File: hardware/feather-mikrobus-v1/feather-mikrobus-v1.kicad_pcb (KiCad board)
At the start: 2 copper layers, 63.5 x 58.4 mm, 26 parts, among them J1 Adafruit_Feather_socket_heade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, J2 Adafruit_Feather_socket_heade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, J3 mikroBUS_socket_header_left_p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, J4 mikroBUS_socket_header_right_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, SW1 C_and_K_JS102011SAQN, SW2 C_and_K_KMR421GULCLFS, SW3 C_and_K_KMR421GULCLFS

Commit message: Add Flying Camp Design logo
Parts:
- added LOGO2: Flying_Camp_Design_logo_30x30mm_silkscreen, Flying_Camp_Design:Flying_Camp_Design_logo_30x30mm_silkscreen, B.Cu at (156.2, 128.3)

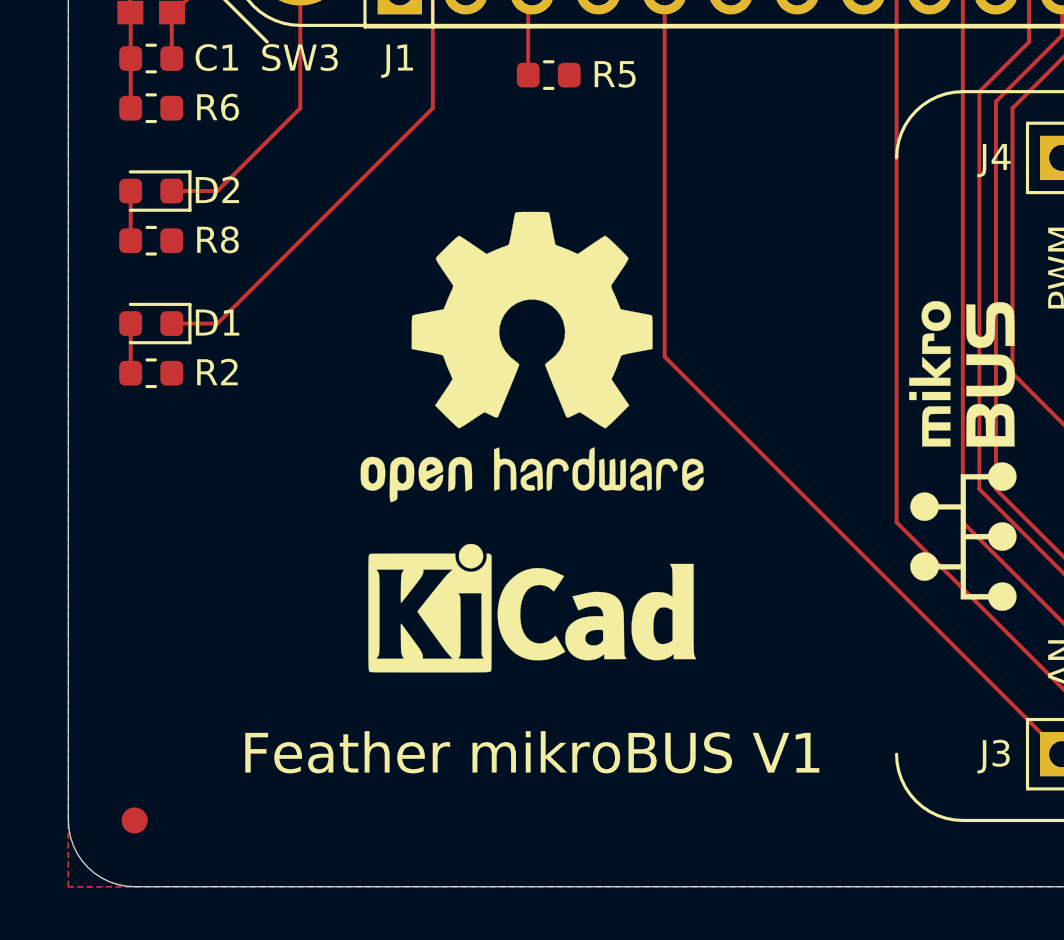
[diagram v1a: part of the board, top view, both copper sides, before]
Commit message: Add Flying Camp Design logos
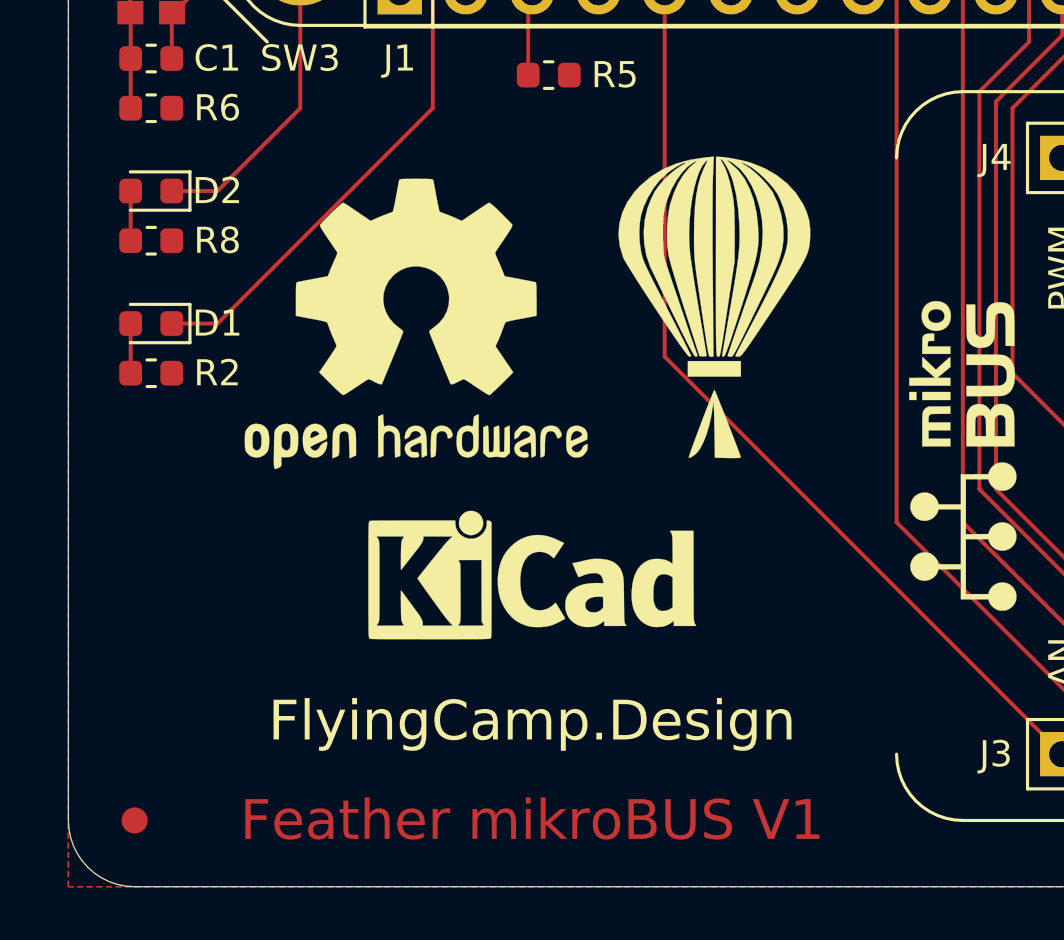
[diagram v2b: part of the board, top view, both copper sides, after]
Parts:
- LOGO2: value Flying_Camp_Design_logo_30x30mm_silkscreen -> Flying_Camp_Design_logo_7.35x11mm_silkscreen; footprint Flying_Camp_Design:Flying_Camp_Design_logo_30x30mm_silkscreen -> Flying_Camp_Design:Flying_Camp_Design_logo_7.35x11mm_silkscreen; moved to F.Cu
- moved LOGO2 10.0 mm to (164.5, 122.6), turned to 0 degrees
- moved REF** 4.62 mm to (153.0, 123.2)
- moved REF** 1.27 mm to (157.5, 133.3)
